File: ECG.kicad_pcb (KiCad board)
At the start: 2 copper layers, 45 parts, among them P1 MountingHole_Pad, P2 MountingHole_Pad, P3 MountingHole_Pad, U1 ADR4525, U2 L7805, U3 INA333, U4 OPA388, U5 OPA388, U6 OPA388

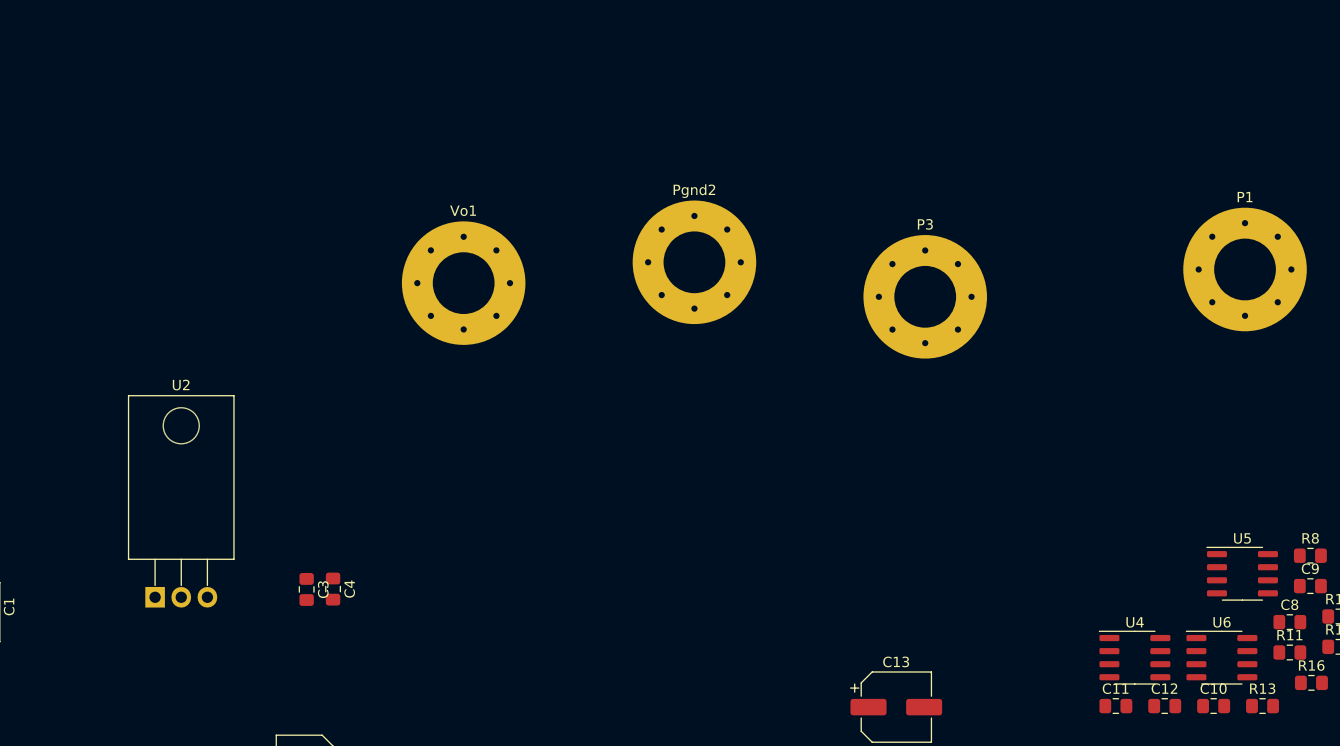
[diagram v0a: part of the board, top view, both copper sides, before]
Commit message: Added battery circuit
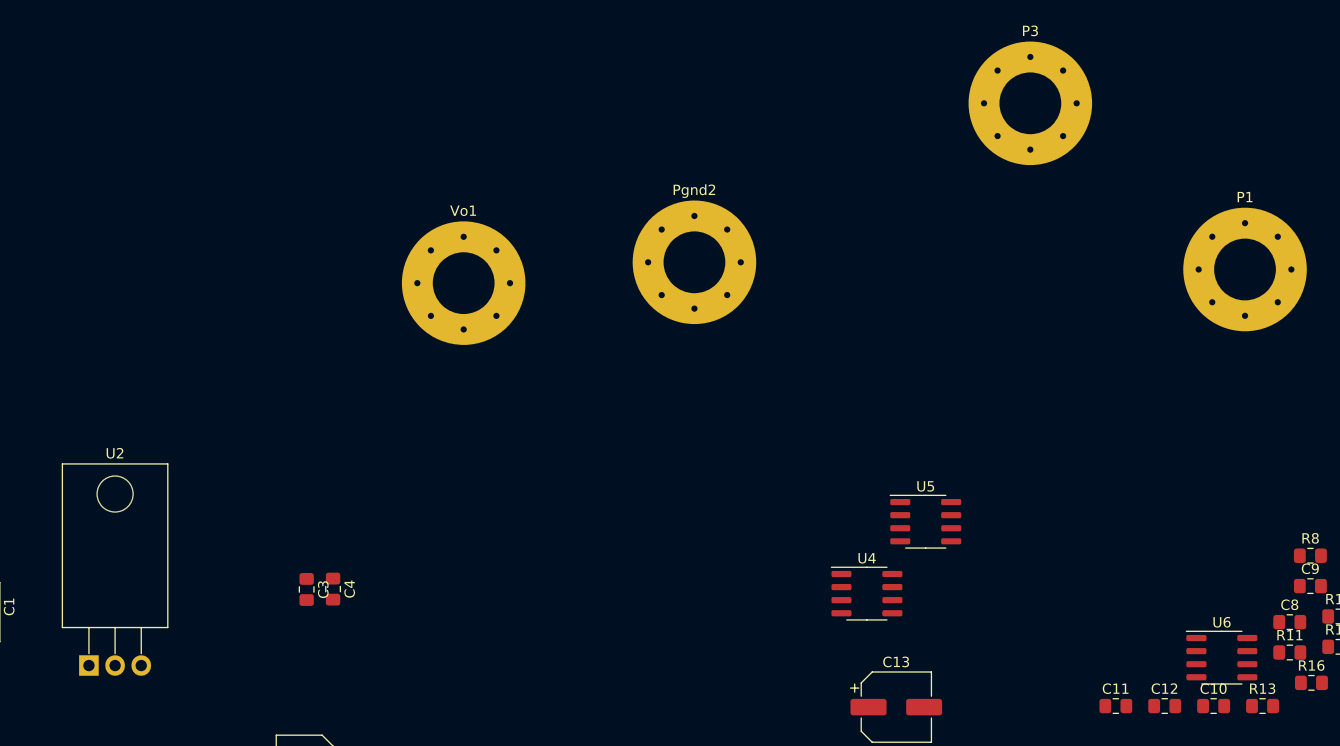
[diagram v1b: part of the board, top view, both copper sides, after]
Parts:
- moved U5 31.2 mm to (155.6, 66.7)
- moved U4 26.8 mm to (149.9, 73.7)
- moved P3 21.4 mm to (165.7, 26.0)
- moved U2 9.23 mm to (74.3, 80.6)
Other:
- net class Default: clearance 0.2 -> 0.1524; trace_width 0.25 -> 0.2032; via_dia 0.8 -> 0.6858; via_drill 0.4 -> 0.3302
- rule trace_clearance: 0.2 -> 0.1524

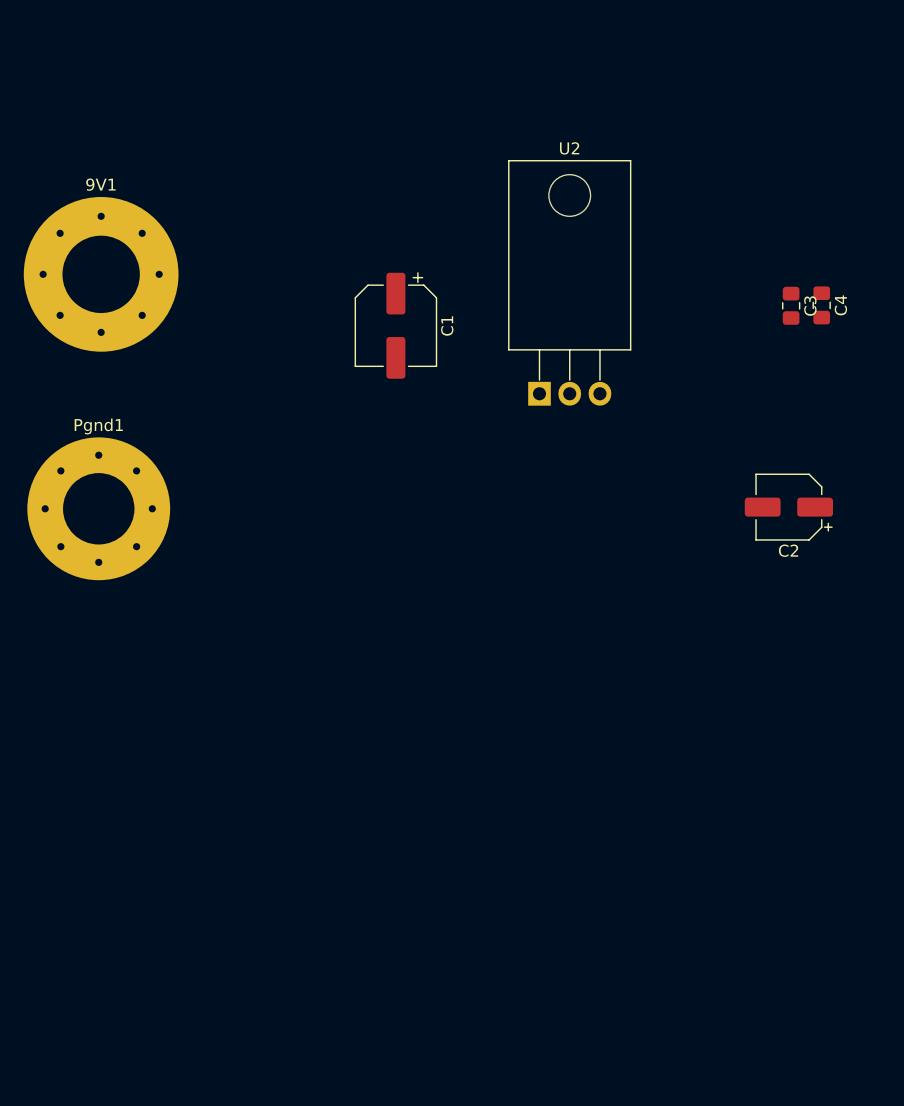
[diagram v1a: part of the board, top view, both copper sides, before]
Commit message: #1 - Create PCB footprints
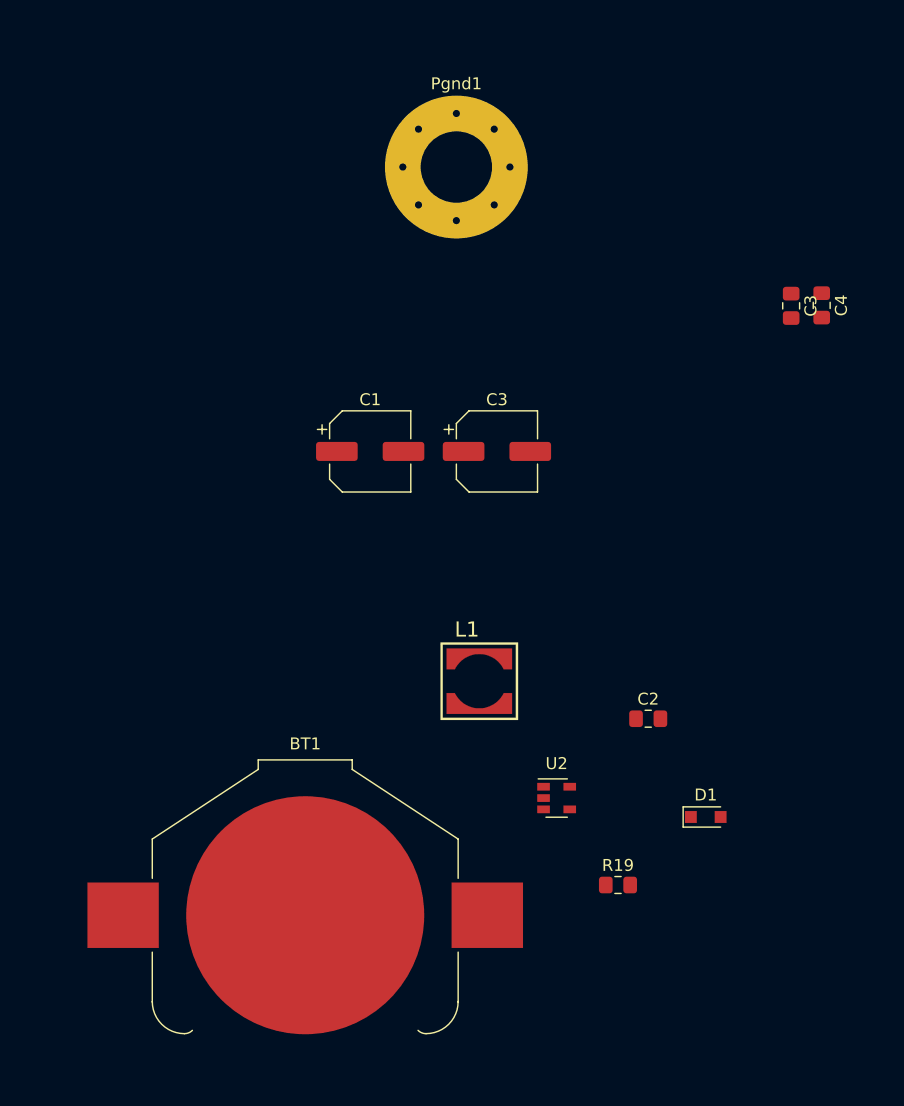
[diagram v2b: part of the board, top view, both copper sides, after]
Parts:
- removed 9V1: MountingHole_Pad, MountingHole:MountingHole_6.5mm_Pad_Via
- added BT1: Battery_Cell, Battery:BatteryHolder_Keystone_3008_1x2450, F.Cu at (54.6, 124.5)
- added C3: 100uF, Capacitor_SMD:CP_Elec_6.3x5.3, F.Cu at (70.7, 85.5)
- added D1: D_Schottky, Diode_SMD:D_SOD-323_HandSoldering, F.Cu at (88.3, 116.2)
- added L1: 10uH, Inductors:L_Sumida_CDRH5D28, F.Cu at (70.5, 106.0)
- added R19: 10, Resistor_SMD:R_0805_2012Metric_Pad1.15x1.40mm_HandSolder, F.Cu at (80.9, 121.9)
- C1: footprint Capacitor_SMD:CP_Elec_6.3x3 -> Capacitor_SMD:CP_Elec_6.3x5.3
- C2: value 10uF -> 1uF; footprint Capacitor_SMD:CP_Elec_5x5.3 -> Capacitor_SMD:C_0805_2012Metric_Pad1.15x1.40mm_HandSolder
- U2: value L7805 -> SP6641; footprint Package_TO_SOT_THT:TO-220-3_Horizontal_TabDown -> Package_TO_SOT_SMD:SOT-23-5
- moved Pgnd1 41.6 mm to (67.3, 61.6)
- moved U2 34.0 mm to (75.7, 114.6)
- moved C2 21.4 mm to (83.4, 108.0), turned to 0 degrees
- moved C1 10.8 mm to (60.1, 85.5), turned to 0 degrees
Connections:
- C1 pad 1: +9V -> Net-(BT1-Pad1)
- C2 pad 1: 5V -> Net-(C2-Pad1)
- U2 pad 1: +9V -> Net-(D1-Pad2)
- U2 pad 3: 5V -> Net-(C2-Pad1)

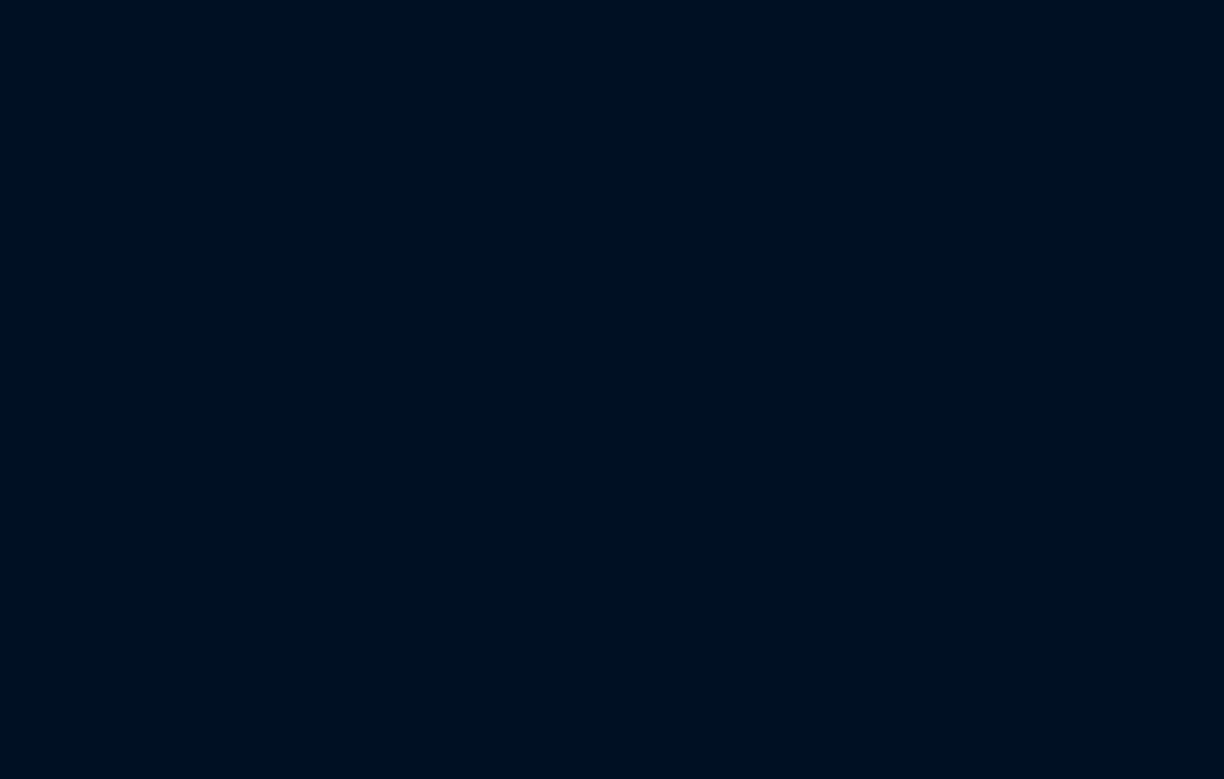
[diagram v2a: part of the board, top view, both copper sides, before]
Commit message: #3 - Add power switch
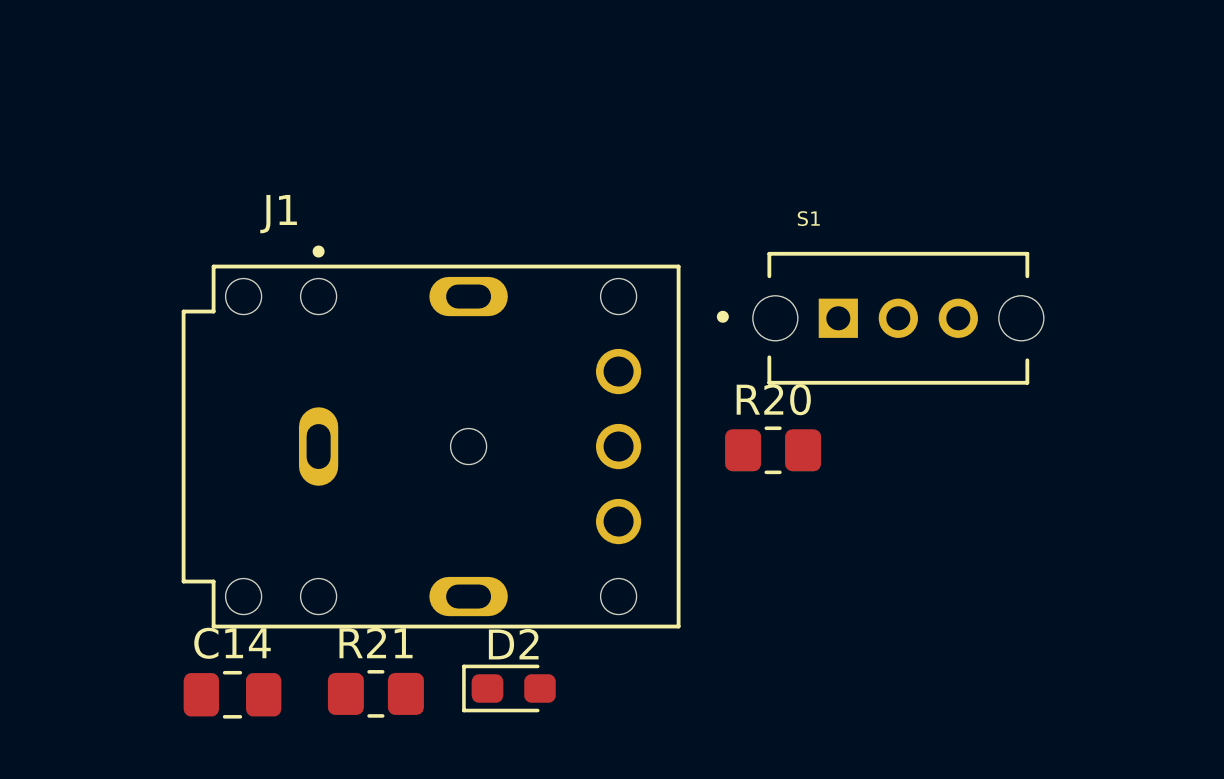
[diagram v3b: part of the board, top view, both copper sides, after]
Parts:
- added C14: 1n, Capacitor_SMD:C_0805_2012Metric_Pad1.18x1.45mm_HandSolder, F.Cu at (77.5, 171.4)
- added D2: LED, Diode_SMD:D_0603_1608Metric_Pad1.05x0.95mm_HandSolder, F.Cu at (86.8, 171.2)
- added J1: SJ-3566AN, Audio:CUI_SJ-3566AN, F.Cu at (85.3, 163.2)
- added R20: 1k, Resistor_SMD:R_0805_2012Metric_Pad1.20x1.40mm_HandSolder, F.Cu at (95.5, 163.3)
- added R21: 220, Resistor_SMD:R_0805_2012Metric_Pad1.20x1.40mm_HandSolder, F.Cu at (82.2, 171.4)
- added S1: OS102011MS2QN1, Switches:SW_OS102011MS2QN1, F.Cu at (99.7, 158.9)
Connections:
- C7 pad 2: /Filters_And_Gain/Vin -> /Probes/Vprobe
- R7 pad 1: /Filters_And_Gain/Vin -> /Probes/Vprobe
- U2 pad 4: Net-(BT1-Pad1) -> SHDN

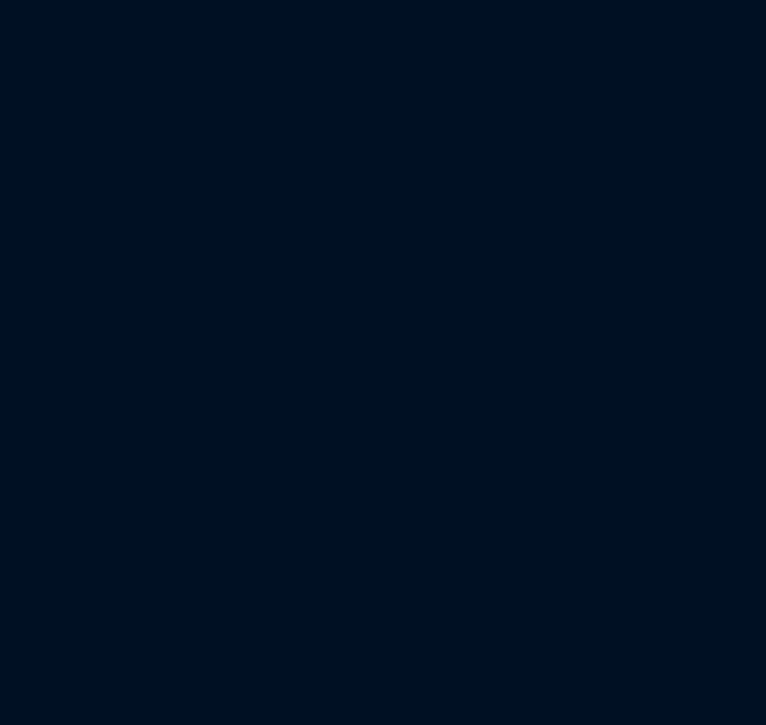
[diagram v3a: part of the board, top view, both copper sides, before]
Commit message: #9 - Add heartbeat indicator
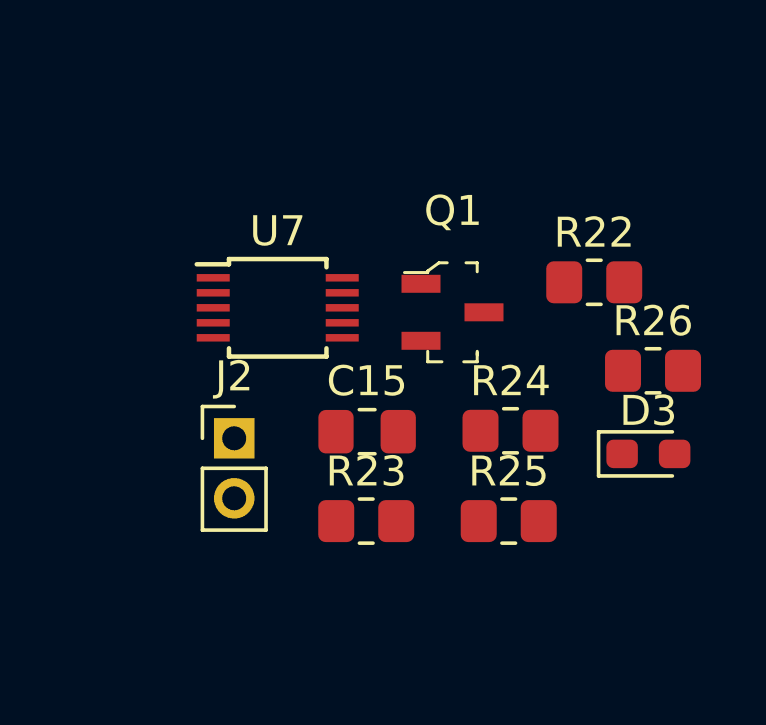
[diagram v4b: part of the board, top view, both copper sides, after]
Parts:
- added C15: 0.1u, Capacitor_SMD:C_0805_2012Metric_Pad1.18x1.45mm_HandSolder, F.Cu at (225.4, 55.9)
- added D3: LED, Diode_SMD:D_0603_1608Metric_Pad1.05x0.95mm_HandSolder, F.Cu at (234.8, 56.6)
- added J2: Conn_01x02_Male, Connector_PinHeader_2.00mm:PinHeader_1x02_P2.00mm_Vertical, F.Cu at (221.0, 56.1)
- added Q1: MMBT3904-7-F, digikey-footprints:SOT-23-3, F.Cu at (228.3, 51.9)
- added R22: 10k, Resistor_SMD:R_0805_2012Metric_Pad1.20x1.40mm_HandSolder, F.Cu at (233.0, 50.9)
- added R23: 10k, Resistor_SMD:R_0805_2012Metric_Pad1.20x1.40mm_HandSolder, F.Cu at (225.4, 58.9)
- added R24: 3.3k, Resistor_SMD:R_0805_2012Metric_Pad1.20x1.40mm_HandSolder, F.Cu at (230.2, 55.9)
- added R25: 3.3k, Resistor_SMD:R_0805_2012Metric_Pad1.20x1.40mm_HandSolder, F.Cu at (230.1, 58.9)
- added R26: 150, Resistor_SMD:R_0805_2012Metric_Pad1.20x1.40mm_HandSolder, F.Cu at (235.0, 53.9)
- added U7: ADS1015IDGS, Package_SO:TSSOP-10_3x3mm_P0.5mm, F.Cu at (222.4, 51.8)
- R21: value 220 -> 100
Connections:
- C7 pad 2: /Probes/Vprobe -> /Filters_And_Gain/Vin
- R18 pad 1: /Filters_And_Gain/Vout -> Vout
- R7 pad 1: /Probes/Vprobe -> /Filters_And_Gain/Vin
- U6 pad 6: /Filters_And_Gain/Vout -> Vout
